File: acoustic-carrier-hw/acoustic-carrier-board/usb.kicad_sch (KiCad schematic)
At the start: 17 parts, among them J4 TYPE-C-31-M-12, Q1 SI2301CDS-T1-GE3, U6 CH340N

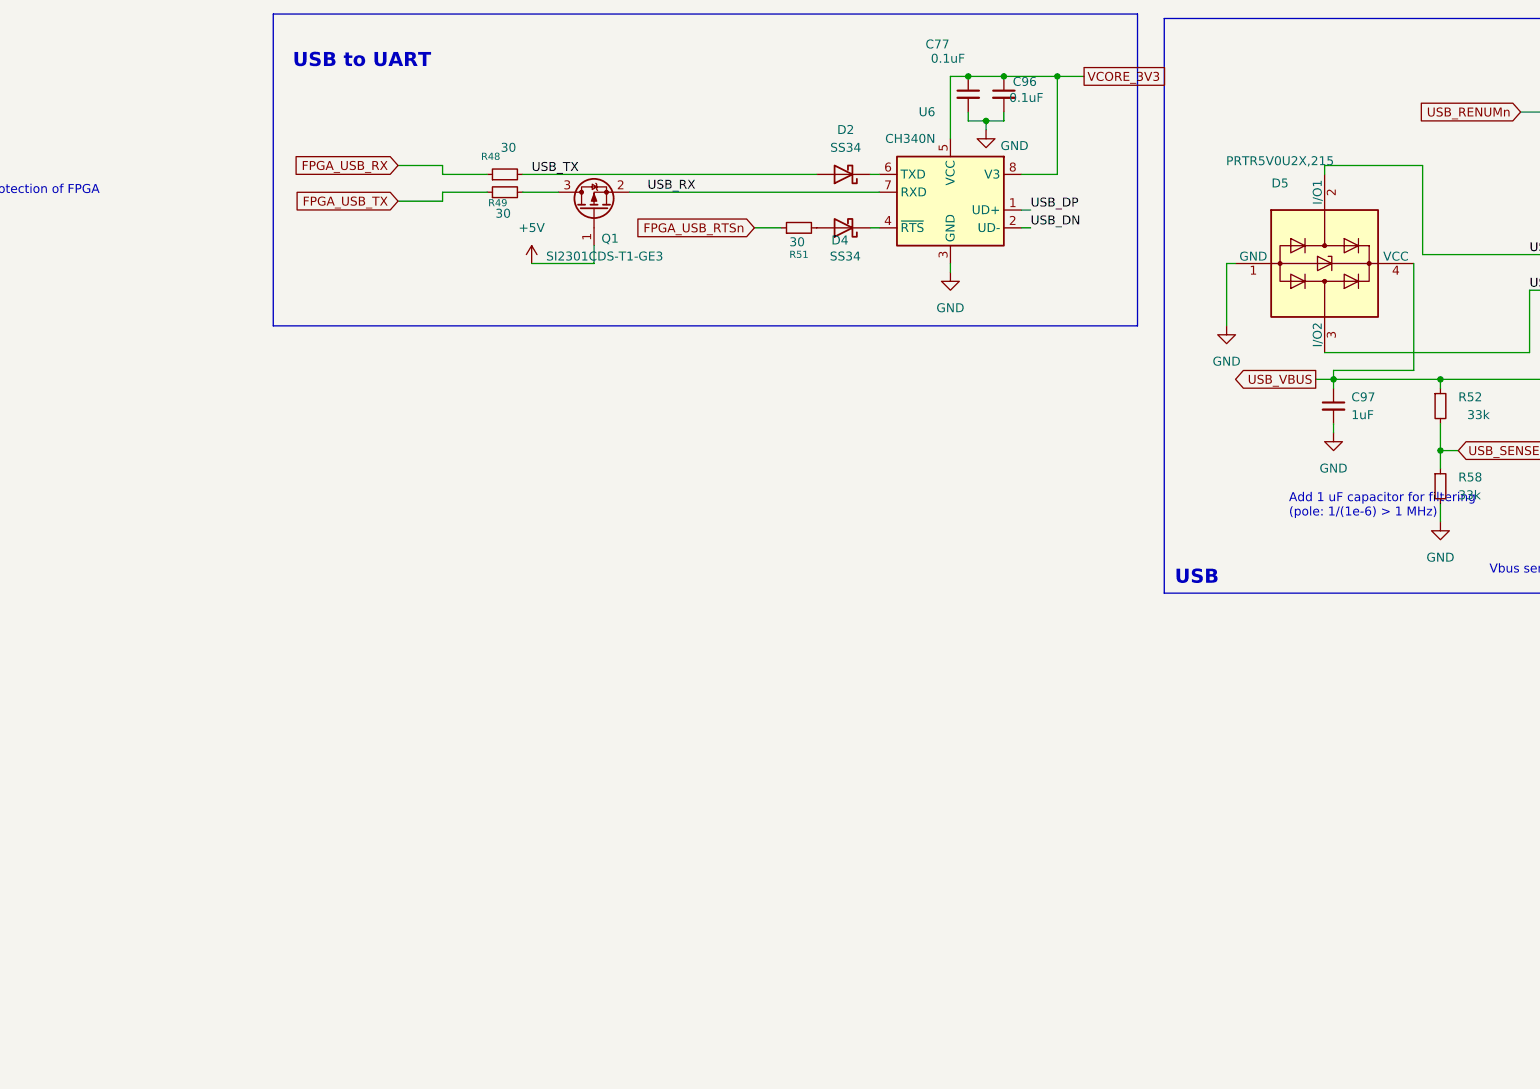
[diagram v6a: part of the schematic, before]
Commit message: [carrier] Worked on USB connector
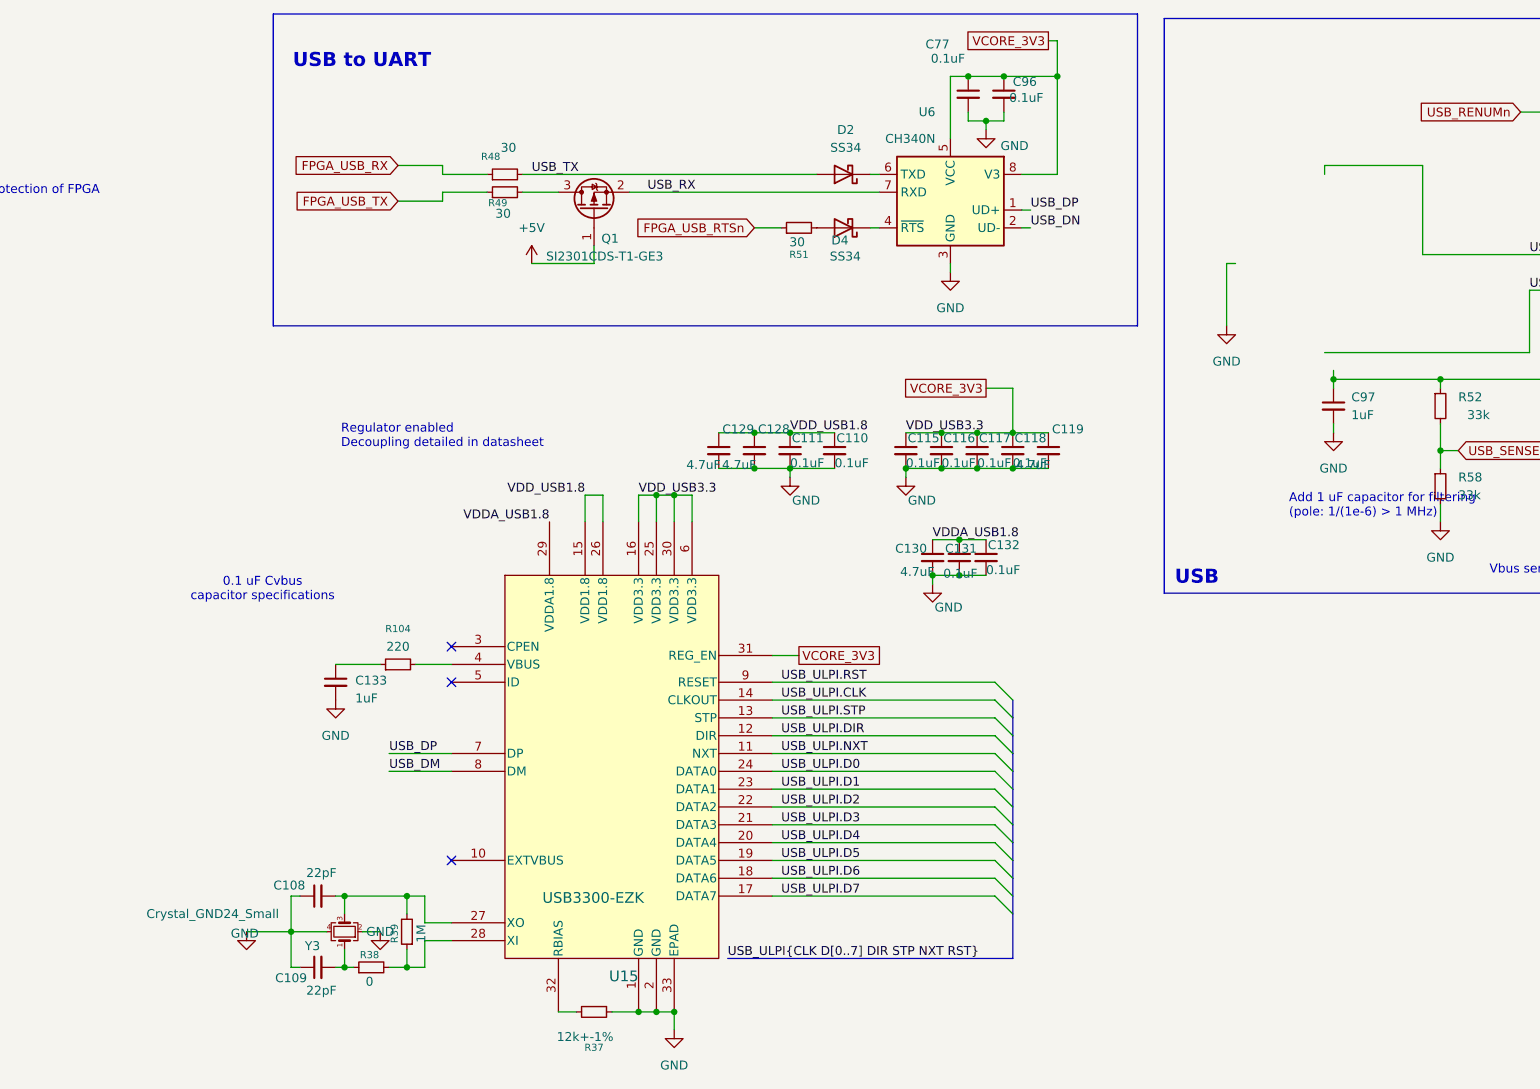
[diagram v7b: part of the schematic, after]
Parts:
- removed D5: PRTR5V0U2X,215, Package_TO_SOT_SMD:SOT-143, symbol Power_Protection:PRTR5V0U2X
- added C108, C109: 22pF, Capacitor_SMD:C_0402_1005Metric, symbol Device:C_Small
- added C110, C111, C115, C116, C117, C118, C131, C132: 0.1uF, Capacitor_SMD:C_0402_1005Metric, symbol Device:C_Small
- added C119, C128, C129, C130: 4.7uF, Capacitor_SMD:C_0402_1005Metric, symbol Device:C_Small
- added C133: 1uF, Capacitor_SMD:C_0805_2012Metric, symbol Device:C_Small
- added R104: 220, Resistor_SMD:R_0603_1608Metric, symbol Device:R_Small
- added R37: 12k+-1%, Resistor_SMD:R_0603_1608Metric, symbol Device:R_Small
- added R38: 0, Resistor_SMD:R_0402_1005Metric_Pad0.72x0.64mm_HandSolder, symbol Device:R_Small
- added R39: 1M, Resistor_SMD:R_0402_1005Metric, symbol Device:R_Small
- added U15: USB3300-EZK, fpga:QFN32_5X5MC_MCH, symbol USB3300-EZK:USB3300-EZK
- added Y3: Crystal_GND24_Small, Crystal:Crystal_SMD_3225-4Pin_3.2x2.5mm, symbol Device:Crystal_GND24_Small
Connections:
- net GND: now also C108.1, C109.1, C110.2, C111.2, C115.2, C116.2, C117.2, C118.2, C119.2, C128.2, C129.2, C130.2, C131.2, C132.2, C133.2, R37.1, U15.1 (GND), U15.2 (GND), U15.33 (EPAD), Y3.2, Y3.4
- net USB_DP: now also U15.7 (DP)
- net VCORE_3V3: now also C115.1, C116.1, C117.1, C118.1, C119.1, U15.16 (VDD3.3), U15.25 (VDD3.3), U15.30 (VDD3.3), U15.31 (REG_EN), U15.6 (VDD3.3)
- net USB_VBUS: no longer names the net of C97.1, J4.A4 (VBUS), J4.A9 (VBUS), J4.B4 (VBUS), J4.B9 (VBUS), R52.1
- new net: R38.2, R39.1, U15.28 (XI)
- new net: C108.2, R39.2, U15.27 (XO), Y3.3
- new net: R37.2, U15.32 (RBIAS)
- new net: C109.2, R38.1, Y3.1
- new net: R104.2, U15.4 (VBUS)
- new net: C133.1, R104.1
- new net USB_DM: U15.8 (DM)
- new net USB_ULPI.CLK: U15.14 (CLKOUT)
- new net USB_ULPI.D0: U15.24 (DATA0)
- new net USB_ULPI.D1: U15.23 (DATA1)
- new net USB_ULPI.D2: U15.22 (DATA2)
- new net USB_ULPI.D3: U15.21 (DATA3)
- new net USB_ULPI.D4: U15.20 (DATA4)
- new net USB_ULPI.D5: U15.19 (DATA5)
- new net USB_ULPI.D6: U15.18 (DATA6)
- new net USB_ULPI.D7: U15.17 (DATA7)
- new net USB_ULPI.DIR: U15.12 (DIR)
- new net USB_ULPI.NXT: U15.11 (NXT)
- new net USB_ULPI.RST: U15.9 (RESET)
- new net USB_ULPI.STP: U15.13 (STP)
- new net VDDA_USB1.8: C130.1, C131.1, C132.1, U15.29 (VDDA1.8)
- new net VDD_USB1.8: C110.1, C111.1, C128.1, C129.1, U15.15 (VDD1.8), U15.26 (VDD1.8)
- no-connect marks 2 -> 5
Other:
- note added: "0.1 uF Cvbus capacitor specifications"
- note added: "Regulator enabled Decoupling detailed in datasheet"

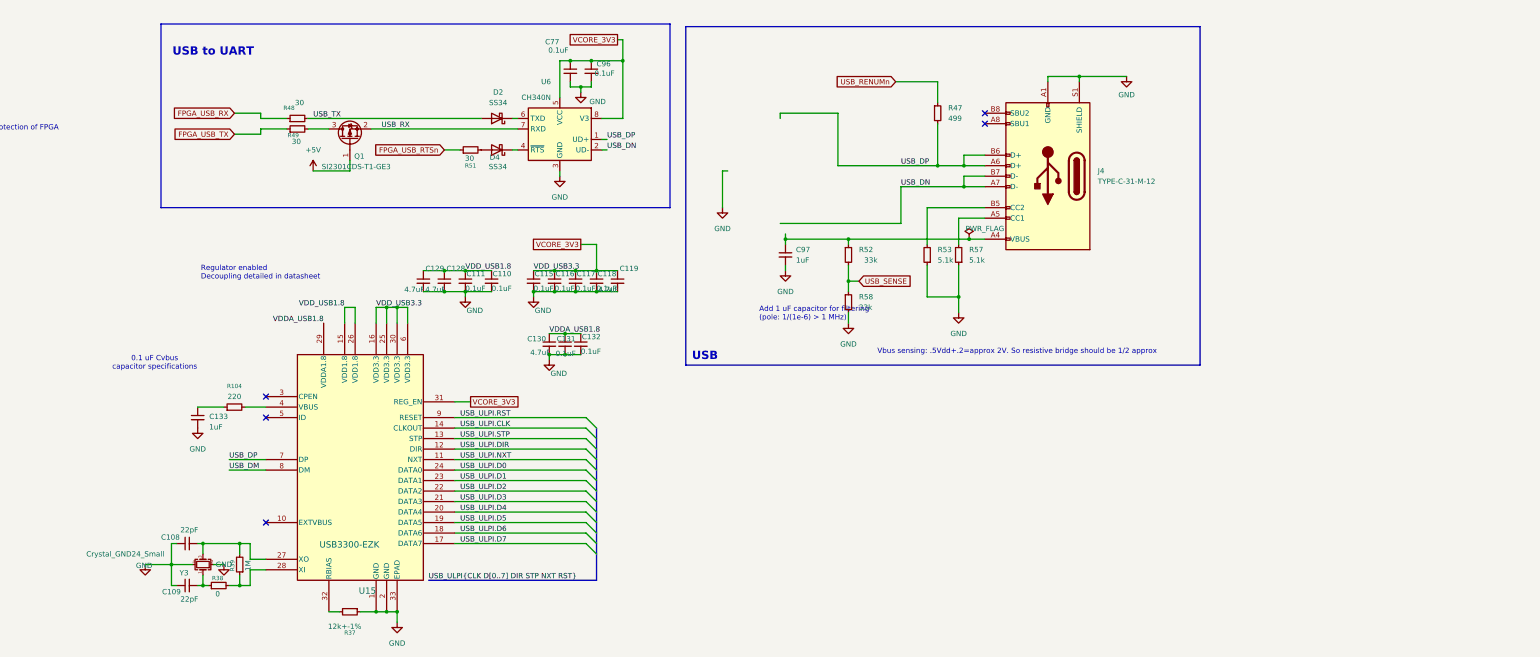
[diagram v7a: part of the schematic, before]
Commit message: [carrier] Doing schmitt trigger calculations and simulations, choosing comparator, choosing USB connector
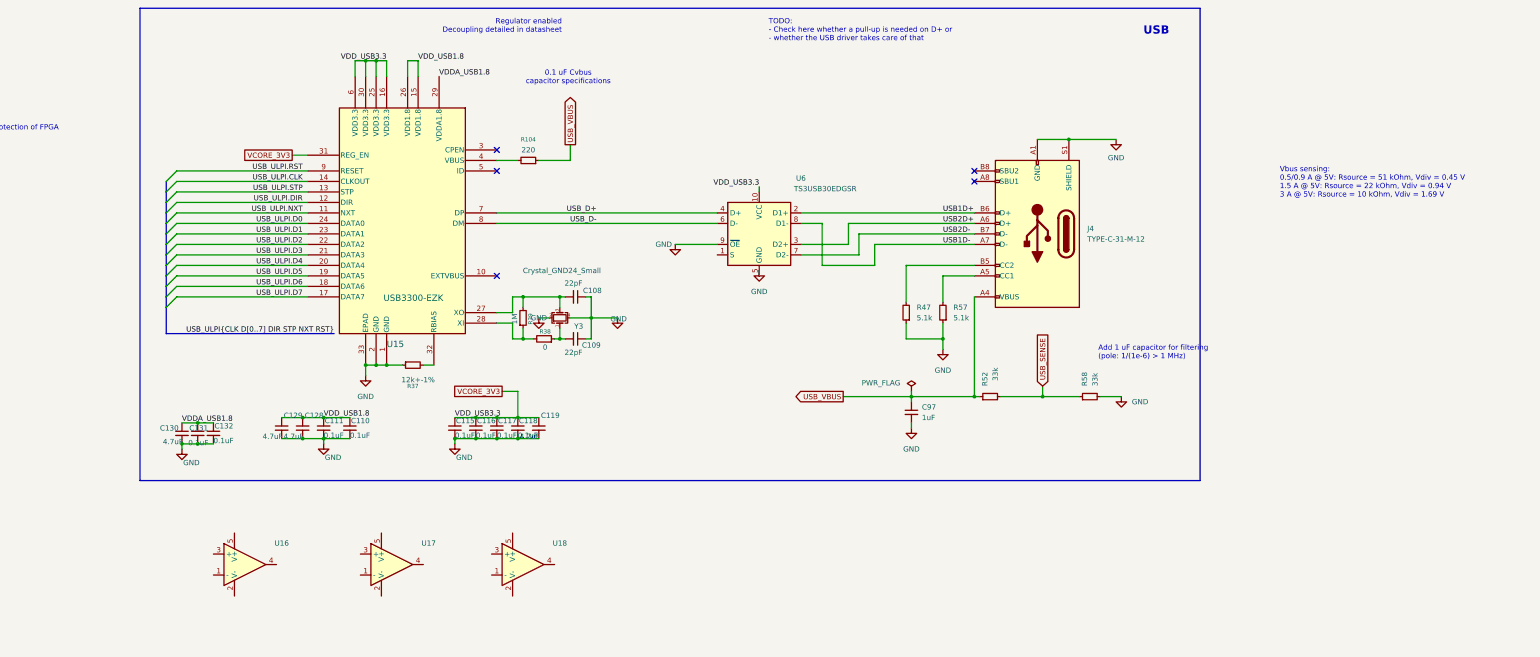
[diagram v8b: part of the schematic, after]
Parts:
- removed C133: 1uF, Capacitor_SMD:C_0805_2012Metric, symbol Device:C_Small
- removed C77, C96: 0.1uF, Capacitor_SMD:C_0402_1005Metric, symbol Device:C_Small
- removed D2, D4: SS34, Diode_SMD:D_SMA, symbol Diode:SS34
- removed Q1: SI2301CDS-T1-GE3, Package_TO_SOT_SMD:SOT-23, symbol Transistor_FET:Si2319CDS
- removed R48, R49, R51: 30, Resistor_SMD:R_0402_1005Metric, symbol Device:R_Small
- removed R53: 5.1k, Resistor_SMD:R_0805_2012Metric, symbol Device:R_Small
- removed U6: CH340N, Package_SO:SOP-8_3.9x4.9mm_P1.27mm, symbol Interface_USB:CH340N
- added U16, U17, U18: ~, Package_TO_SOT_SMD:SOT-23-5, symbol COS3201:COS3201
- added U6: TS3USB30EDGSR, Package_SO:VSSOP-10_3x3mm_P0.5mm, symbol Interface_USB:TS3USB30EDGSR
- J4: MPN (none) -> TYPE-C-31-M-12; Manufacturing part number TYPE-C-31-M-12 -> (none)
- R47: value 499 -> 5.1k; footprint Resistor_SMD:R_0402_1005Metric -> Resistor_SMD:R_0805_2012Metric; LPN C4125 -> C27834; Manufacturing part number 0402WGF4990TCE -> 0805W8F5101T5E
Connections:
- net USB_RENUMn is gone; now on net GND: R47.1
- net GND: now also U6.5 (GND), U6.9 (~{OE})
- net VCORE_3V3: now also U6.10 (VCC)
- net USB_VBUS: now reaches C97.1, J4.A4 (VBUS), J4.A9 (VBUS), J4.B4 (VBUS), J4.B9 (VBUS), R52.1
- net USB_VBUS: now also R104.1
- net at J4.B5 (CC2): now also R47.2
- net USB_DM renamed USB_D-
- net USB_D-: now also U6.6 (D-)
- net USB_DN renamed USB1D-
- net USB1D-: now also U6.8 (D1-); no longer J4.B7 (D-)
- removed net USB_DP: J4.A6 (D+), J4.B6 (D+), R47.2, U15.7 (DP)
- new net USB1D+: J4.B6 (D+), U6.2 (D1+)
- new net USB2D+: J4.A6 (D+), U6.3 (D2+)
- new net USB2D-: J4.B7 (D-), U6.7 (D2-)
- new net USB_D+: U15.7 (DP), U6.4 (D+)
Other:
- note added: "TODO: - Check here whether a pull-up is needed on D+ or - whether the USB driver takes care of that"
- note added: "Vbus sensing: 0.5/0.9 A @ 5V: Rsource = 51 kOhm, Vdiv = 0.45 V 1.5 A @ 5V: Rsource = 22 kOhm, Vdiv = 0.94 V 3 A @ 5V: Rsource = 10 kOhm, Vdiv = 1.69 V"
- note removed: "Vbus sensing: .5Vdd+.2=approx 2V. So resistive bridge should be 1/2 approx"
- moved on the sheet: C108, C109, C110, C111, C115, C116, C117, C118, C119, C128, C129, C130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
